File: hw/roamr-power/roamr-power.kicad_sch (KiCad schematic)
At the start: 0 parts

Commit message: reorganizing to roamr-power
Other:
- title: ROAMR power -> ROAMR power board
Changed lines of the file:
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@@
 	(paper "USLetter")
 	(title_block
-		(title "ROAMR power")
+		(title "ROAMR power board")
 		(date "2026-01-18")
 		(rev "1.0")
@@
 		)
 		(instances
-			(project "roamr"
+			(project "roamr-power"
 				(path "/bfe84b16-3df2-48dd-882e-523c3a68f778"
 					(page "3")
@@
 		)
 		(instances
-			(project "roamr"
+			(project "roamr-power"
 				(path "/bfe84b16-3df2-48dd-882e-523c3a68f778"
 					(page "4")
@@
 		)
 		(instances
-			(project "roamr"
+			(project "roamr-power"
 				(path "/bfe84b16-3df2-48dd-882e-523c3a68f778"
 					(page "5")
@@
 		)
 		(instances
-			(project "roamr"
+			(project "roamr-power"
 				(path "/bfe84b16-3df2-48dd-882e-523c3a68f778"
 					(page "2")

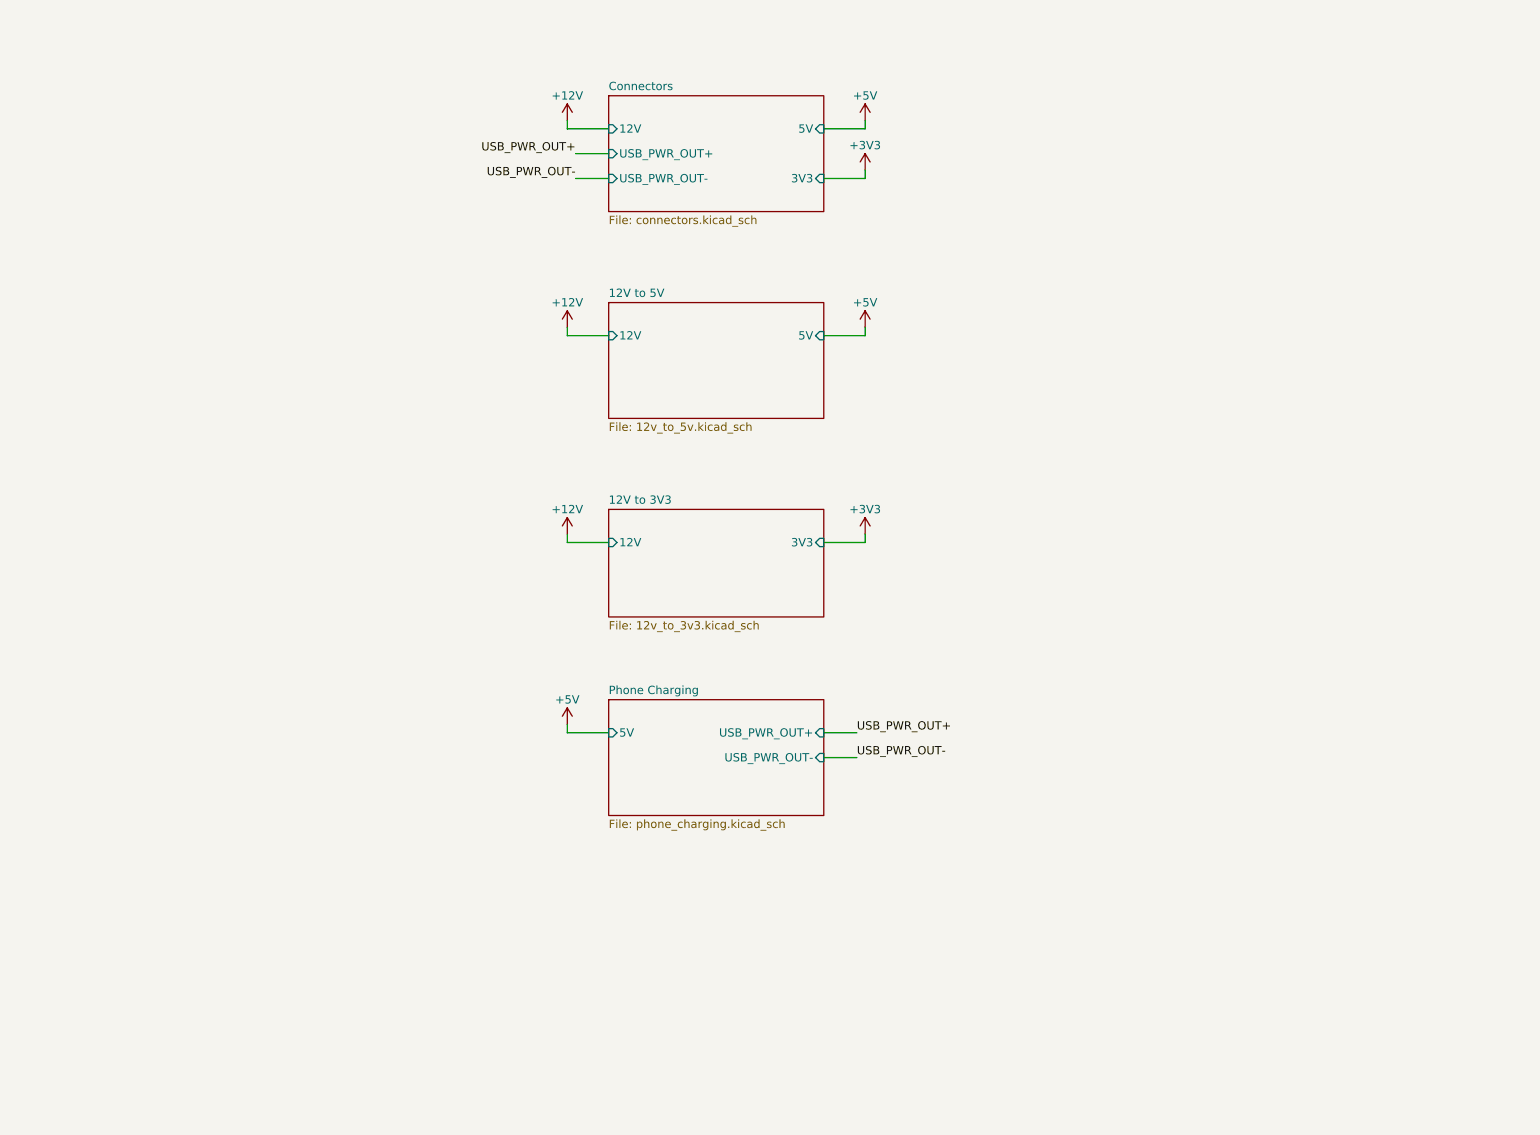
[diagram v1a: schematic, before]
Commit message: mostly finished power, probably need a bit of drawing cleanup, for schematic
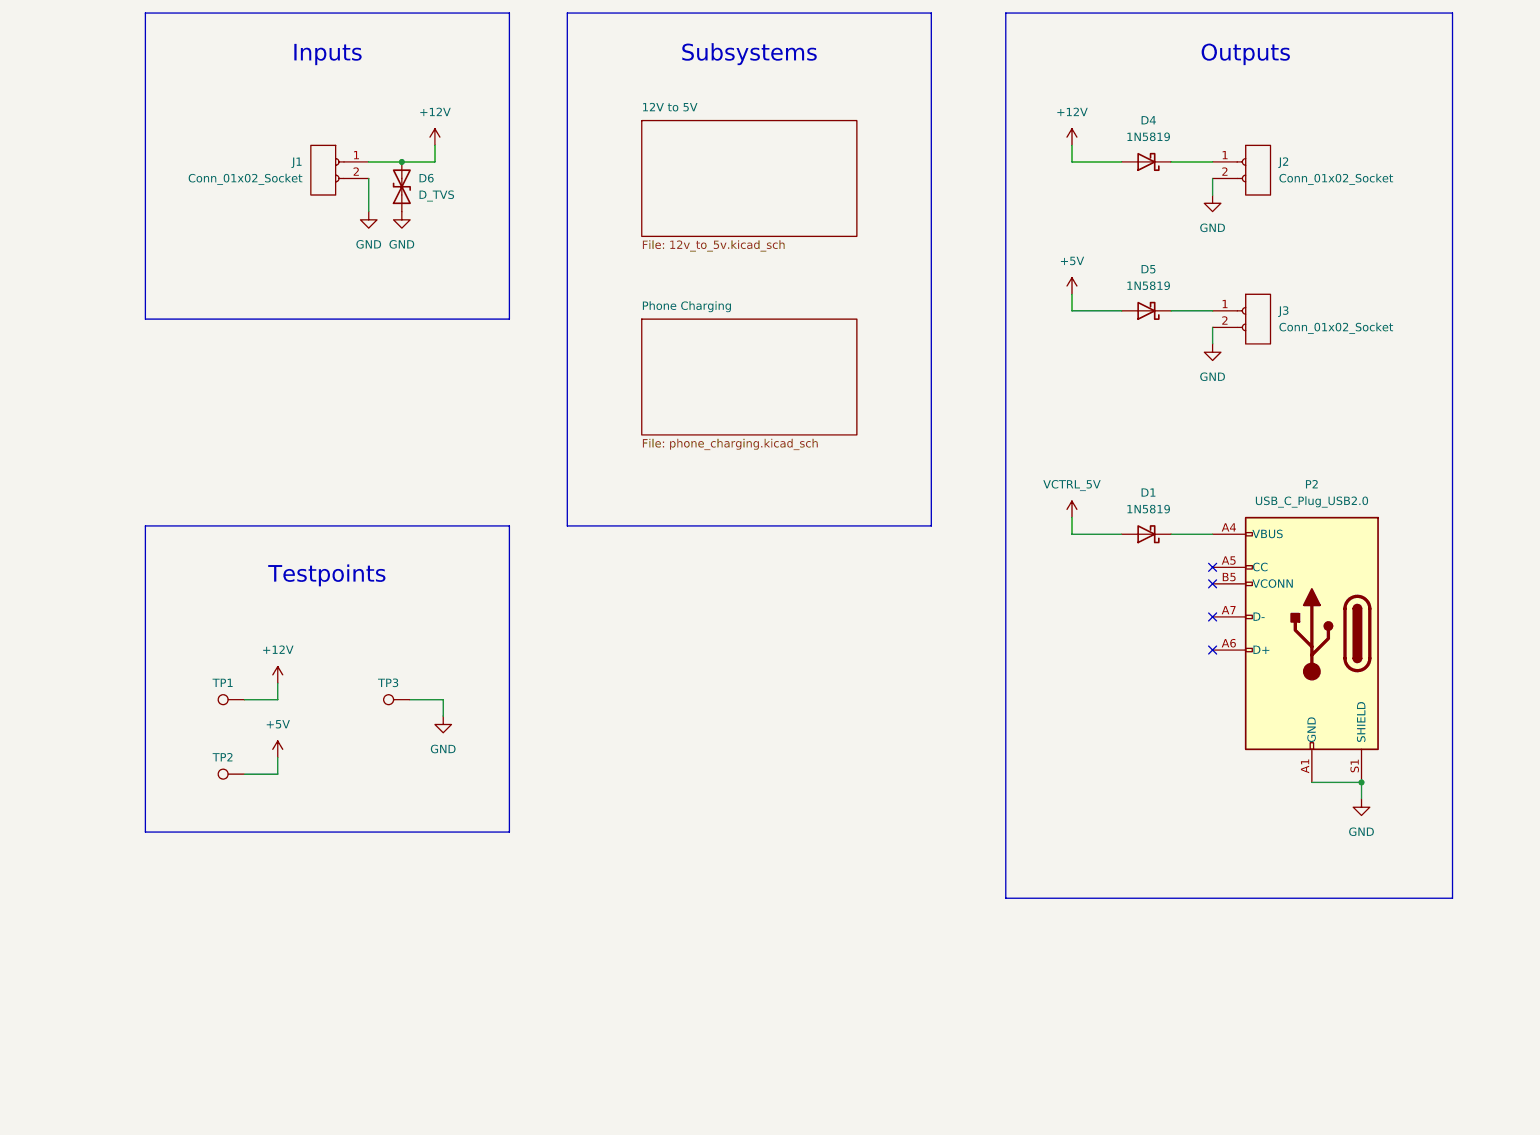
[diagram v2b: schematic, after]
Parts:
- added D1, D4, D5: 1N5819, Diode_THT:D_DO-41_SOD81_P10.16mm_Horizontal, symbol Diode:1N5819
- added D6: D_TVS, symbol Device:D_TVS
- added J1, J2, J3: Conn_01x02_Socket, symbol Connector:Conn_01x02_Socket
- added P2: USB_C_Plug_USB2.0, symbol Connector:USB_C_Plug_USB2.0
- added TP1, TP2, TP3: TestPoint, symbol Connector:TestPoint
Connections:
- net +12V: now also D4.2 (A), D6.2 (A2), J1.1 (Pin_1), TP1.1
- net +5V: now also D5.2 (A), TP2.1
- new net: D4.1 (K), J2.1 (Pin_1)
- new net: D5.1 (K), J3.1 (Pin_1)
- new net: D1.1 (K), P2.A4 (VBUS), P2.A9 (VBUS), P2.B4 (VBUS), P2.B9 (VBUS)
- new net GND: D6.1 (A1), J1.2 (Pin_2), J2.2 (Pin_2), J3.2 (Pin_2), P2.A1 (GND), P2.A12 (GND), P2.B1 (GND), P2.B12 (GND), P2.S1 (SHIELD), TP3.1
- new net VCTRL_5V: D1.2 (A)
- no-connect marks 0 -> 4
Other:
- removed sheet 12V to 3V3
- removed sheet Connectors
- sheet 12V to 5V ports: added none; removed 12V, 5V
- sheet Phone Charging ports: added none; removed 5V, USB_PWR_OUT+, USB_PWR_OUT-
- note added: "Inputs"
- note added: "Outputs"
- note added: "Subsystems"
- note added: "Testpoints"

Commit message: fixed after nathan's rereview
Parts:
- added TP4: TestPoint, symbol Connector:TestPoint
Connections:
- net VCTRL_5V: now also TP4.1
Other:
- company: (none) -> Mechatronics FYDP Group 16
- moved on the sheet: D6, TP3

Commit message: picked the BOM and added two more indicator LEDs for the 12V and 5V rails
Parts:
- D6: footprint (none) -> SMLJ12A-R:DIOM7959X262N
- J1: footprint (none) -> TB002-500-02BE:TB00250002BE
- J2, J3: footprint (none) -> Connector_JST:JST_XH_S2B-XH-A-1_1x02_P2.50mm_Horizontal
- P2: footprint (none) -> USB4125-GF-A:CONN6_USB4125_GCT
- TP1, TP2, TP4: footprint (none) -> TestPoint:TestPoint_Pad_D1.5mm
- TP3: footprint (none) -> TestPoint:TestPoint_Keystone_5005-5009_Compact
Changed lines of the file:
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@@
 			)
 		)
-		(property "Footprint" ""
+		(property "Footprint" "SMLJ12A-R:DIOM7959X262N"
 			(at 82.55 50.8 0)
 			(effects
@@
 			)
 		)
-		(property "Footprint" ""
+		(property "Footprint" "TestPoint:TestPoint_Pad_D1.5mm"
 			(at 83.82 123.19 0)
 			(effects
@@
 			)
 		)
-		(property "Footprint" ""
+		(property "Footprint" "Connector_JST:JST_XH_S2B-XH-A-1_1x02_P2.50mm_Horizontal"
 			(at 212.09 45.72 0)
 			(effects
@@
 			)
 		)
-		(property "Footprint" ""
+		(property "Footprint" "Connector_JST:JST_XH_S2B-XH-A-1_1x02_P2.50mm_Horizontal"
 			(at 212.09 68.58 0)
 			(effects
@@
 			)
 		)
-		(property "Footprint" ""
+		(property "Footprint" "TB002-500-02BE:TB00250002BE"
 			(at 72.39 45.72 0)
 			(effects
@@
 			)
 		)
-		(property "Footprint" ""
+		(property "Footprint" "USB4125-GF-A:CONN6_USB4125_GCT"
 			(at 218.44 118.11 0)
 			(effects
@@
 			)
 		)
-		(property "Footprint" ""
+		(property "Footprint" "TestPoint:TestPoint_Pad_D1.5mm"
 			(at 58.42 134.62 0)
 			(effects
@@
 			)
 		)
-		(property "Footprint" ""
+		(property "Footprint" "TestPoint:TestPoint_Pad_D1.5mm"
 			(at 58.42 123.19 0)
 			(effects
@@
 			)
 		)
-		(property "Footprint" ""
+		(property "Footprint" "TestPoint:TestPoint_Keystone_5005-5009_Compact"
 			(at 83.82 134.62 0)
 			(effects

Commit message: layout
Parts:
- P2: footprint USB4125-GF-A:CONN6_USB4125_GCT -> USB4125-GF-A:USB4125GFA
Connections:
- net 12V_OUT: now reaches D4.1 (K), J2.1 (Pin_1)
- net 5V_OUT: now reaches D5.1 (K), J3.1 (Pin_1)
- net USB_OUT: now reaches D1.1 (K), P2.A4 (VBUS), P2.A9 (VBUS), P2.B4 (VBUS), P2.B9 (VBUS)
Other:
- moved on the sheet: D1, D4, D5
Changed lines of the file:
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@@
 	(wire
 		(pts
-			(xy 185.42 68.58) (xy 193.04 68.58)
+			(xy 185.42 68.58) (xy 189.23 68.58)
 		)
 		(stroke
@@
 	(wire
 		(pts
-			(xy 185.42 102.87) (xy 193.04 102.87)
-		)
-		(stroke
-			(width 0)
-			(type default)
-		)
-	)
-	(wire
-		(pts
-			(xy 200.66 102.87) (xy 207.01 102.87)
-		)
-		(stroke
-			(width 0)
-			(type default)
-		)
-	)
-	(wire
-		(pts
-			(xy 200.66 68.58) (xy 207.01 68.58)
+			(xy 185.42 102.87) (xy 189.23 102.87)
+		)
+		(stroke
+			(width 0)
+			(type default)
+		)
+	)
+	(wire
+		(pts
+			(xy 196.85 102.87) (xy 207.01 102.87)
+		)
+		(stroke
+			(width 0)
+			(type default)
+		)
+	)
+	(wire
+		(pts
+			(xy 196.85 68.58) (xy 207.01 68.58)
 		)
 		(stroke
@@
 	(wire
 		(pts
-			(xy 185.42 45.72) (xy 193.04 45.72)
+			(xy 185.42 45.72) (xy 189.23 45.72)
 		)
 		(stroke
@@
 	(wire
 		(pts
-			(xy 200.66 45.72) (xy 207.01 45.72)
+			(xy 196.85 45.72) (xy 207.01 45.72)
 		)
 		(stroke
@@
 			(width 0)
 			(type default)
+		)
+	)
+	(label "12V_OUT"
+		(at 198.12 45.72 0)
+		(effects
+			(font
+				(size 1.27 1.27)
+			)
+			(justify left bottom)
+		)
+	)
+	(label "5V_OUT"
+		(at 198.12 68.58 0)
+		(effects
+			(font
+				(size 1.27 1.27)
+			)
+			(justify left bottom)
+		)
+	)
+	(label "USB_OUT"
+		(at 198.12 102.87 0)
+		(effects
+			(font
+				(size 1.27 1.27)
+			)
+			(justify left bottom)
 		)
 	)
@@
 			)
 		)
-		(property "Footprint" "USB4125-GF-A:CONN6_USB4125_GCT"
+		(property "Footprint" "USB4125-GF-A:USB4125GFA"
 			(at 218.44 118.11 0)
 			(effects
@@
 	(symbol
 		(lib_id "Diode:1N5819")
-		(at 196.85 102.87 180)
+		(at 193.04 102.87 180)
 		(unit 1)
 		(exclude_from_sim no)
@@
 		(fields_autoplaced yes)
 		(property "Reference" "D1"
-			(at 197.1675 96.52 0)
+			(at 193.3575 96.52 0)
 			(effects
 				(font
@@
 		)
 		(property "Value" "1N5819"
-			(at 197.1675 99.06 0)
+			(at 193.3575 99.06 0)
 			(effects
 				(font
@@
 		)
 		(property "Footprint" "Diode_THT:D_DO-41_SOD81_P10.16mm_Horizontal"
-			(at 196.85 98.425 0)
+			(at 193.04 98.425 0)
 			(effects
 				(font
@@
 		)
 		(property "Datasheet" "http://www.vishay.com/docs/88525/1n5817.pdf"
-			(at 196.85 102.87 0)
+			(at 193.04 102.87 0)
 			(effects
 				(font
@@
 		)
 		(property "Description" "40V 1A Schottky Barrier Rectifier Diode, DO-41"
-			(at 196.85 102.87 0)
+			(at 193.04 102.87 0)
 			(effects
 				(font
@@
 	(symbol
 		(lib_id "Diode:1N5819")
-		(at 196.85 68.58 180)
+		(at 193.04 68.58 180)
 		(unit 1)
 		(exclude_from_sim no)
@@
 		(fields_autoplaced yes)
 		(property "Reference" "D5"
-			(at 197.1675 62.23 0)
+			(at 193.3575 62.23 0)
 			(effects
 				(font
@@
 		)
 		(property "Value" "1N5819"
-			(at 197.1675 64.77 0)
+			(at 193.3575 64.77 0)
 			(effects
 				(font
@@
 		)
 		(property "Footprint" "Diode_THT:D_DO-41_SOD81_P10.16mm_Horizontal"
-			(at 196.85 64.135 0)
+			(at 193.04 64.135 0)
 			(effects
 				(font
@@
 		)
 		(property "Datasheet" "http://www.vishay.com/docs/88525/1n5817.pdf"
-			(at 196.85 68.58 0)
+			(at 193.04 68.58 0)
 			(effects
 				(font
@@
 		)
 		(property "Description" "40V 1A Schottky Barrier Rectifier Diode, DO-41"
-			(at 196.85 68.58 0)
+			(at 193.04 68.58 0)
 			(effects
 				(font
@@
 	(symbol
 		(lib_id "Diode:1N5819")
-		(at 196.85 45.72 180)
+		(at 193.04 45.72 180)
 		(unit 1)
 		(exclude_from_sim no)
@@
 		(fields_autoplaced yes)
 		(property "Reference" "D4"
-			(at 197.1675 39.37 0)
+			(at 193.3575 39.37 0)
 			(effects
 				(font
@@
 		)
 		(property "Value" "1N5819"
-			(at 197.1675 41.91 0)
+			(at 193.3575 41.91 0)
 			(effects
 				(font
@@
 		)
 		(property "Footprint" "Diode_THT:D_DO-41_SOD81_P10.16mm_Horizontal"
-			(at 196.85 41.275 0)
+			(at 193.04 41.275 0)
 			(effects
 				(font
@@
 		)
 		(property "Datasheet" "http://www.vishay.com/docs/88525/1n5817.pdf"
-			(at 196.85 45.72 0)
+			(at 193.04 45.72 0)
 			(effects
 				(font
@@
 		)
 		(property "Description" "40V 1A Schottky Barrier Rectifier Diode, DO-41"
-			(at 196.85 45.72 0)
-			(effects
-				(font
+			(at 193.04 45.72 0)
+			(effects
+				(font

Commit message: pcb schematic and layout updated
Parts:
- removed D1, D4, D5: 1N5819, Diode_THT:D_DO-41_SOD81_P10.16mm_Horizontal, symbol Diode:1N5819
- added D1, D4, D5: PMEG3050EP,115, PMEG3050EP:PMEG3050EP115, symbol PMEG3050EP_115:PMEG3050EP,115
- added R11: 510R, Resistor_SMD:R_0603_1608Metric, symbol Device:R_US
- added R12, R13: 10kR, Resistor_SMD:R_0603_1608Metric, symbol Device:R_US
- added R14: 7.5kR, Resistor_SMD:R_0603_1608Metric, symbol Device:R_US
- added R15: 56kR, Resistor_SMD:R_0603_1608Metric, symbol Device:R_US
- added SW2: SW_SPDT, OS102011MS2QN1:OS102011MA1QN1, symbol Switch:SW_SPDT
- added U3: TPS259541DSGR, TPS259541DSGR:SON50P200X200X80-9N, symbol TPS259541DSGR:TPS259541DSGR
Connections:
- net 12V_OUT: now also D4.1 (K)
- net 5V_OUT: now also D5.1 (K)
- net GND: now also R11.2, R12.1, R14.2, U3.8 (GND), U3.9 (PAD)
- net USB_OUT: now also D1.1 (K), R15.1
- net at P2.A5 (CC): now also R15.2
- net +12V renamed VIN_12V
- net VIN_12V: now also SW2.2 (B), U3.3 (IN_1), U3.4 (IN_2); no longer TP1.1
- net +5V renamed VSYS_5V
- net VSYS_5V: now also D5.2 (A)
- net VCTRL_5V renamed VLIM_5V
- net VLIM_5V: now also D1.2 (A)
- new net: R12.2, U3.6 (~{FLT})
- new net: R11.1, U3.7 (ILM)
- new net: R13.1, SW2.3 (C)
- new net VSYS_12V: D4.2 (A), TP1.1, U3.5 (OUT)
- new net VSYS_EN: R13.2, R14.1, U3.2 (EN/UVLO)
- no-connect marks 4 -> 5
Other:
- note added: "Input Control"
- moved on the sheet: D6, J1, J2, J3, P2, TP1, TP2, TP3, TP4

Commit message: final edits
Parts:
- removed J2, J3: Conn_01x02_Socket, Connector_JST:JST_XH_S2B-XH-A-1_1x02_P2.50mm_Horizontal, symbol Connector:Conn_01x02_Socket
- removed P2: USB_C_Plug_USB2.0, USB4125-GF-A:USB4125GFA, symbol Connector:USB_C_Plug_USB2.0
- added J2, J3: JST_XH_S2B-XH-A-1, Connector_JST:JST_XH_S2B-XH-A-1_1x02_P2.50mm_Horizontal, symbol Connector:Conn_01x02_Pin
- added J4: USB4125-GF-A, USB4125-GF-A:USB4125GFA, symbol USB4125-GF-A:USB4125-GF-A
- added R16: 56kR, Resistor_SMD:R_0603_1608Metric, symbol Device:R_US
- D6: value D_TVS -> SMLJ13A; footprint SMLJ12A-R:DIOM7959X262N -> SMLJ13CA-R:DIOM7959X262N; Manufacturer_Part_Number (none) -> SMLJ12A
- J1: value Conn_01x02_Socket -> TB002-500-02BE; Manufacturer_Part_Number (none) -> TB002-500-02BE
- SW2: value SW_SPDT -> OS102011MS2QN1; Manufacturer_Part_Number (none) -> OS102011MS2QN1
- TP3: Manufacturer_Part_Number (none) -> 5005-5009
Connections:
- net 12V_OUT: now also J2.1 (Pin_1)
- net 5V_OUT: now also J3.1 (Pin_1)
- net GND: now also J2.2 (Pin_2), J3.2 (Pin_2), J4.A12 (GND), J4.B12 (GND)
- net USB_OUT: now also J4.A9 (VBUS), J4.B4 (VBUS), J4.B9 (VBUS), R16.1
- net at R15.2: now also J4.A5 (CC1)
- new net: J4.B5 (CC2), R16.2
- no-connect marks 5 -> 2
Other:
- moved on the sheet: R15

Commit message: final save
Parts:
- D6: Manufacturer_Part_Number SMLJ12A -> SMLJ13A
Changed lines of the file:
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@@
 			)
 		)
-		(property "Manufacturer_Part_Number" "SMLJ12A"
+		(property "Manufacturer_Part_Number" "SMLJ13A"
 			(at 66.04 50.8 90)
 			(effects
